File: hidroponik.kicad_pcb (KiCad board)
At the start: 2 copper layers, 115.5 x 66 mm, 14 parts, among them J1 Barrel_Jack, J2 LM2596_IN, J3 ESP32_Right, J4 DS18B20_Waterproof, J5 DHT22_TempHumidity, J6 pH_Sensor_Module, J7 TDS_Sensor_Module, J8 ESP32_LEFT, J9 LM2596_OUT

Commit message: update: sensor ph dan tds
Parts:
- moved J7 36.3 mm to (124.0, 113.0)
- moved J6 36.0 mm to (124.0, 94.5)
- moved F2 5.62 mm to (113.7, 79.0)
- moved J1 4.25 mm to (113.5, 124.3)
- moved R1 3.00 mm to (131.7, 86.5)
- moved D1 2.17 mm to (127.7, 76.0)
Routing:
- net /+5V: track 234.6 -> 195.7 mm
- net /PH_ANALOG: track 49.3 -> 13.1 mm
- net /GND: track 254.7 -> 220.2 mm
- net /TDS_ANALOG: track 55.2 -> 26.2 mm
- net /+12V_IN: track 108.0 -> 101.4 mm
- net /+12V_FUSED: track 5.17 -> 8.86 mm
- net /EN: track 15.4 -> 17.5 mm
- net /+12V_PROTECTED: track 16.0 -> 17.7 mm
- net /+3V3: track 141.9 -> 143.0 mm

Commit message: update: lm2596 dan pencocokan datasheet
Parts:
- moved J2 8.50 mm to (153.0, 78.0)
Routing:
- net /GND: track 220.2 -> 211.7 mm
- net /+12V_PROTECTED: track 17.7 -> 26.2 mm
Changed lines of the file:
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@@
 	(footprint "Connector_PinHeader_2.54mm:PinHeader_1x02_P2.54mm_Vertical"
 		(layer "F.Cu")
-		(at 144.5 78)
+		(at 153 78)
 		(descr "Through hole straight pin header, 1x02, 2.54mm pitch, single row")
 		(tags "Through hole pin header THT 1x02 2.54mm single row")
@@
 	)
 	(segment
+		(start 154.96 82.5)
+		(end 167.04 82.5)
+		(width 0.2)
+		(layer "F.Cu")
+		(net "/GND")
+	)
+	(segment
 		(start 184 126.5)
 		(end 184 131)
@@
 	)
 	(segment
-		(start 144.5 80.54)
-		(end 146.46 82.5)
-		(width 0.2)
-		(layer "F.Cu")
-		(net "/GND")
-	)
-	(segment
 		(start 124 115.54)
 		(end 125.46 115.54)
@@
 	)
 	(segment
-		(start 146.46 82.5)
-		(end 167.04 82.5)
+		(start 153 80.54)
+		(end 154.96 82.5)
 		(width 0.2)
 		(layer "F.Cu")
@@
 	(segment
 		(start 129.66 78)
-		(end 144.5 78)
+		(end 153 78)
 		(width 0.2)
 		(layer "F.Cu")

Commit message: update: kaki ph, tds dan wiring
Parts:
- moved J6 17.5 mm to (106.5, 95.5)
- moved J7 17.5 mm to (106.5, 112.5)
- moved J1 6.30 mm to (119.8, 124.5)
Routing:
- net /+12V_IN: track 101.4 -> 73.1 mm
- net /+5V: track 195.7 -> 213.0 mm
- net /PH_ANALOG: track 13.1 -> 29.7 mm
- net /GND: track 211.7 -> 221.8 mm
- net /TDS_ANALOG: track 26.2 -> 34.7 mm
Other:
- board size 115.5 x 66 mm -> 119 x 69 mm

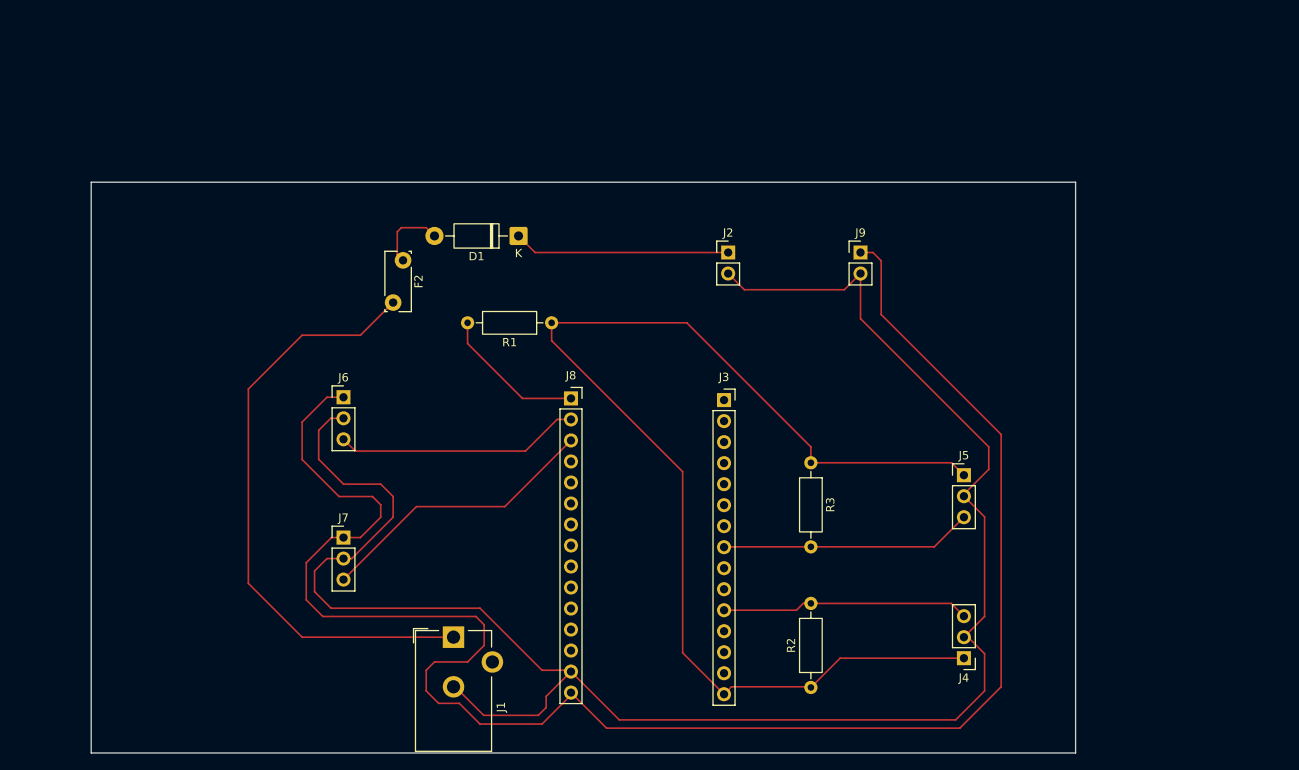
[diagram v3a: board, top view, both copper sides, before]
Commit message: feat: add pin for ultrasonik
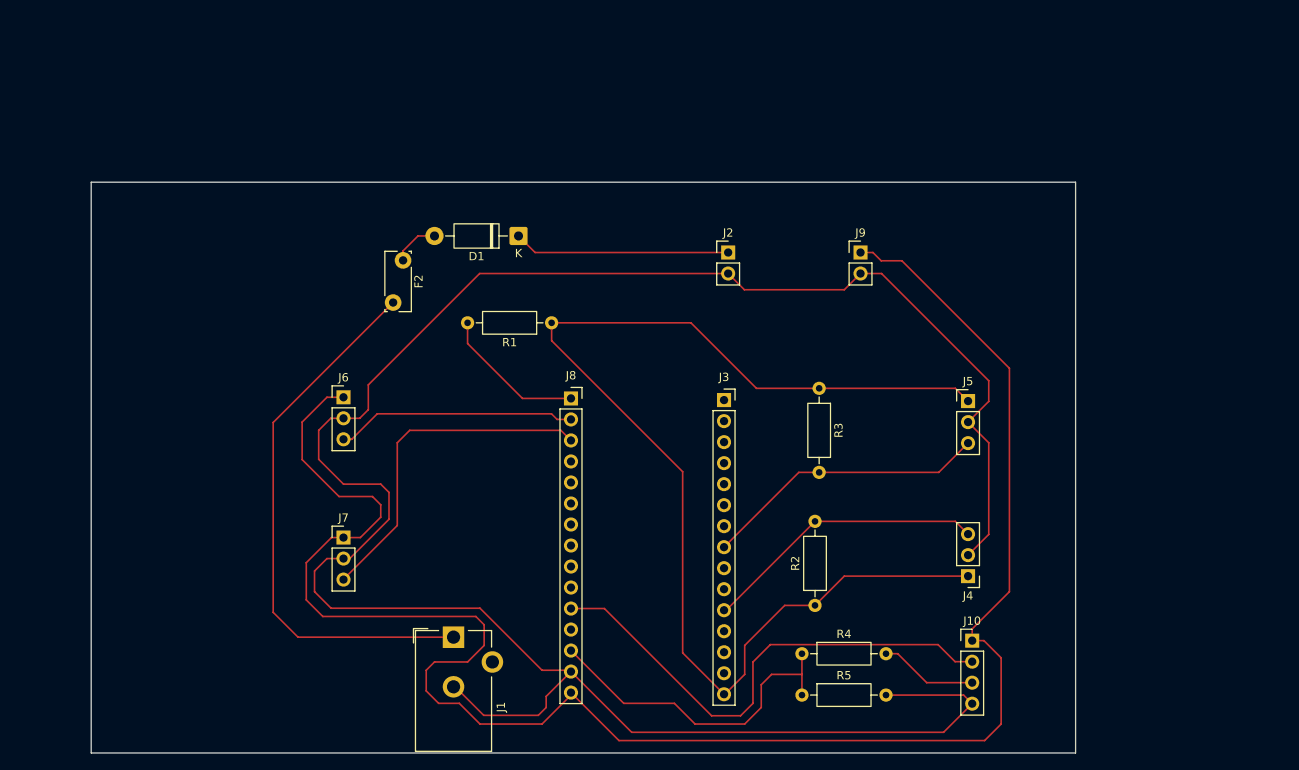
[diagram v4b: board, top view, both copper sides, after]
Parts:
- added J10: HC-SR04, Connector_PinHeader_2.54mm:PinHeader_1x04_P2.54mm_Vertical, F.Cu at (182.5, 124.9)
- added R4: 1k, Resistor_THT:R_Axial_DIN0207_L6.3mm_D2.5mm_P10.16mm_Horizontal, F.Cu at (161.9, 126.5)
- added R5: 2k, Resistor_THT:R_Axial_DIN0207_L6.3mm_D2.5mm_P10.16mm_Horizontal, F.Cu at (161.9, 131.5)
- moved R2 9.93 mm to (163.5, 120.7)
- moved J4 9.93 mm to (182.0, 117.1)
- moved R3 9.06 mm to (164.0, 94.4)
- moved J5 8.97 mm to (182.0, 96.0)
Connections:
- J8 pad 11: unconnected-(J8-Pin_11-Pad11) -> /TRIG
- J8 pad 13: unconnected-(J8-Pin_13-Pad13) -> /ECHO_ESP32
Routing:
- net /TRIG: track 0.00 -> 61.2 mm
- net /GND: track 221.8 -> 270.7 mm
- net /ECHO_ESP32: track 0.00 -> 40.7 mm
- net /ECHO_RAW: track 0.00 -> 11.9 mm
- net /+5V: track 213.0 -> 222.9 mm
- net /TDS_ANALOG: track 34.7 -> 41.6 mm
- net /+12V_IN: track 73.1 -> 66.8 mm
- net /DS18B20_DATA: track 30.0 -> 34.6 mm
- net /DHT22_DATA: track 30.5 -> 34.7 mm
- net /+12V_FUSED: track 8.86 -> 5.70 mm
- net /+3V3: track 143.0 -> 145.3 mm
- net /PH_ANALOG: track 29.7 -> 29.1 mm

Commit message: feat: add hole
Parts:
- added REF**: MountingHole_3.2mm_M3, MountingHole:MountingHole_3.2mm_M3, F.Cu at (190.5, 134.0)
- added REF**: MountingHole_3.2mm_M3, MountingHole:MountingHole_3.2mm_M3, F.Cu at (80.5, 134.0)
- added REF**: MountingHole_3.2mm_M3, MountingHole:MountingHole_3.2mm_M3, F.Cu at (190.5, 74.0)
- added REF**: MountingHole_3.2mm_M3, MountingHole:MountingHole_3.2mm_M3, F.Cu at (80.5, 74.0)
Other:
- board text added: "NZPS"
- board text added: "https://github.com/ALZEE23"

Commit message: refactor: wiring
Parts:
- moved J9 40.3 mm to (208.0, 67.7)
- moved REF** 32.0 mm to (215.5, 54.0)
- moved REF** 25.0 mm to (215.5, 134.5)
- moved REF** 21.9 mm to (71.5, 54.0)
- moved J2 12.4 mm to (146.0, 67.7)
- moved J6 12.3 mm to (94.2, 96.5)
- moved J7 12.3 mm to (94.2, 113.5)
- moved J1 11.1 mm to (108.8, 124.3)
- moved REF** 9.00 mm to (71.5, 134.0)
- moved J8 6.75 mm to (127.2, 95.8)
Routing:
- net /GND: track 270.7 -> 348.9 mm
- net /+5V: track 222.9 -> 241.9 mm
- net /+12V_IN: track 66.8 -> 79.4 mm
- net /TRIG: track 61.2 -> 69.0 mm
- net /ECHO_ESP32: track 40.7 -> 47.4 mm
- net /EN: track 17.8 -> 11.7 mm
- net /PH_ANALOG: track 29.1 -> 34.4 mm
- net /+12V_PROTECTED: track 26.2 -> 21.8 mm
- net /TDS_ANALOG: track 41.6 -> 45.6 mm
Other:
- board size 119 x 69 mm -> 153 x 89 mm
